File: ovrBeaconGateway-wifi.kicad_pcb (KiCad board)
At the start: 2 copper layers, 78 x 78 mm, 39 parts, among them J1 USB_MICROB_RA_LONG, J2 CONN_RJ45_RA, Q1 BJT_NPN_1.5A_25V, Q2 BJT_NPN_1.5A_25V, Q3 FET_NP_5A/3A_60V, U1 SILICONLABS_SI7050, U2 TOREX_XC6210, U3 FTDI_RT232RL, U4 ESP32-WROOM, U5 INTERSIL_ISL32602EFBZ

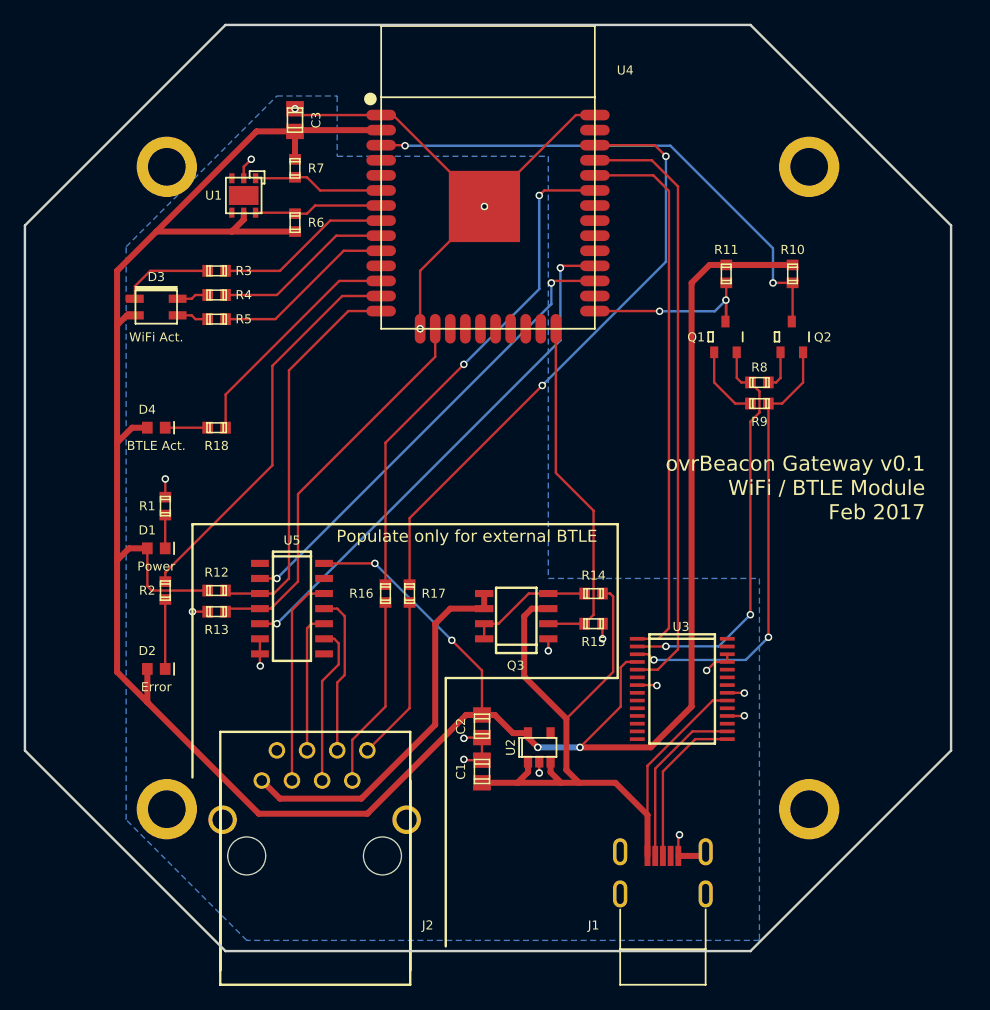
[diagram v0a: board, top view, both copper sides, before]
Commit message: Included an optional BLE121 on this module to allow for stand-alone long range operation
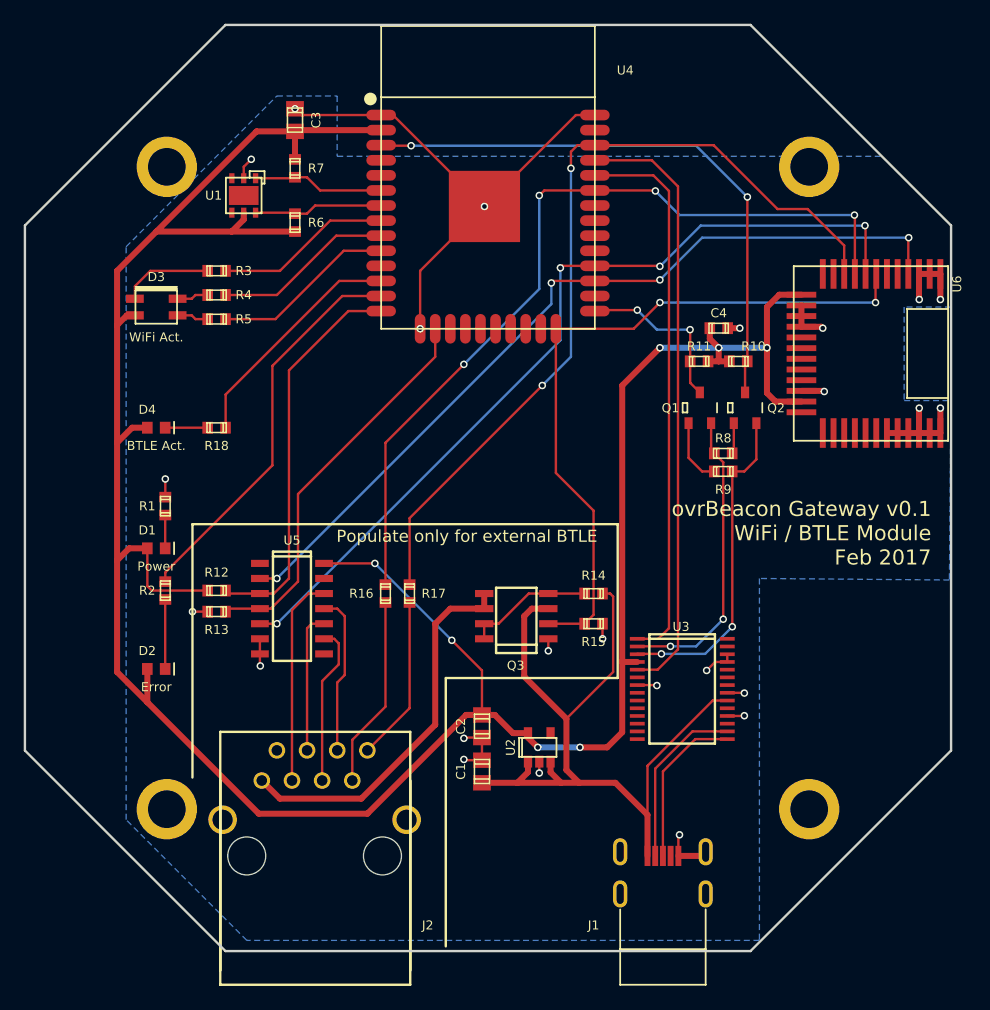
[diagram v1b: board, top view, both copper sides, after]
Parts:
- added C4: C_0.1uF_10v_0603, ovrEngineered:C_0603, F.Cu at (146.4, 62.7)
- added U6: BLUEGIGA_BLE121, ovrEngineered:BLE121, F.Cu at (165.1, 58.4)
- moved R10 8.67 mm to (148.1, 65.5), turned to 180 degrees
- moved R11 7.71 mm to (144.8, 65.5), turned to 0 degrees
- moved Q2 7.15 mm to (147.7, 70.7)
- moved R8 6.70 mm to (146.8, 73.3)
- moved R9 6.48 mm to (146.8, 74.8)
- moved Q1 6.35 mm to (143.9, 70.7)
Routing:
- net /ESP32-TX_BTLE-RX: track 39.6 -> 70.6 mm, vias 2 -> 4
- net /BTLE_POWER_ENABLE: track 29.5 -> 59.8 mm, vias 0 -> 2
- net /ESP32-RX_BTLE-TX: track 44.3 -> 72.5 mm, vias 2 -> 4
- net /ESP32-RTS_BTLE-CTS: track 43.0 -> 70.7 mm, vias 2 -> 4
- net GND: track 71.2 -> 92.7 mm, vias 17 -> 24
- net /ESP32-CTS_BTLE-RTS: track 51.4 -> 71.2 mm
- net Net-(Q2-Pad2): track 37.9 -> 27.6 mm
- net Net-(Q1-Pad2): track 34.3 -> 25.1 mm
- net /ESP32_EN: track 44.5 -> 49.3 mm
- net /ESP32_IO0: track 16.5 -> 14.4 mm
- net +3V3: track 231.0 -> 232.4 mm, vias 4 -> 7
- net Net-(Q1-Pad1): track 6.33 -> 5.56 mm
- net Net-(Q2-Pad1): track 3.34 -> 2.60 mm

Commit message: Initial commit of second revision changes
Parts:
- removed D3: CREE_CLV1A_FKB, ovrEngineered:CREE_CLV1A_FKB
- removed D4: LED_BLUE_0603, ovrEngineered:D_0603
- added J3: CONN_DBG_PDI, ovrEngineered:TC2030-IDC, F.Cu at (142.2, 51.6)
- added J4: CONN_1.27MM_5X2, ovrEngineered:20021111-00010T4LF, F.Cu at (151.1, 91.4)
- added R19: R_0_0603, ovrEngineered:R_0603, F.Cu at (144.8, 77.7)
- added R20: R_0_0603, ovrEngineered:R_0603, F.Cu at (146.3, 77.7)
- added R21: R_0_0603, ovrEngineered:R_0603, F.Cu at (109.5, 84.1)
- added R22: R_0_0603, ovrEngineered:R_0603, F.Cu at (151.9, 62.0)
- added REF**: LIGHTPIPE_VLP-XXX, ovrEngineered:LIGHTPIPE_VLP-XXX, F.Cu at (99.9, 61.0)
- added REF**: LIGHTPIPE_VLP-XXX, ovrEngineered:LIGHTPIPE_VLP-XXX, F.Cu at (99.8, 71.1)
- added REF**: LIGHTPIPE_VLP-XXX, ovrEngineered:LIGHTPIPE_VLP-XXX, F.Cu at (99.9, 91.3)
- added SW1: ESWITCH_TL3315NF100Q, ovrEngineered:TL3315NF100Q, F.Cu at (99.9, 81.3)
- added U7: LITEON_LTR-329ALS, ovrEngineered:LITEON_LTR-329ALS, F.Cu at (99.9, 91.4)
- D1: value LED_GREEN_0603 -> CREE_CLV1A_FKB; footprint ovrEngineered:D_0603 -> ovrEngineered:CREE_CLV1A_FKB
- D2: value LED_RED_0603 -> CREE_CLV1A_FKB; footprint ovrEngineered:D_0603 -> ovrEngineered:CREE_CLV1A_FKB
- J1, J2: moved to B.Cu
- R1: value R_402_1%_0603 -> R_12K_1%_0603
- R11: value R_5.1K_1%_0603 -> R_12K_1%_0603
- R18: value R_402_1%_0603 -> R_10K_1%_0603
- R6, R7: value R_10K_1%_0603 -> R_402_1%_0603
- moved R18 48.1 mm to (151.9, 65.3), turned to 0 degrees
- moved U1 45.2 mm to (99.9, 96.3), turned to 90 degrees
- moved D2 30.5 mm to (99.9, 61.0)
- moved R2 22.1 mm to (106.9, 63.9), turned to 180 degrees
- moved U6 20.0 mm to (156.0, 76.2)
- moved Q1 19.7 mm to (134.1, 87.9)
- moved Q2 18.4 mm to (141.0, 87.9)
- moved R14 17.9 mm to (118.0, 84.1), turned to 270 degrees
- moved R8 16.8 mm to (138.4, 87.9)
- moved R15 16.5 mm to (119.8, 84.1), turned to 270 degrees
- moved C2 16.1 mm to (130.4, 111.9)
- moved R9 14.3 mm to (138.4, 86.4)
- moved R1 14.2 mm to (106.9, 65.4), turned to 180 degrees
- moved C1 13.4 mm to (132.7, 111.9), turned to 90 degrees
- moved R17 12.6 mm to (107.8, 84.1)
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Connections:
- net /+5V_SWITCHED renamed Net-(J2-Pad1)
- D1 pad 1: +3V3 -> Net-(D1-Pad1)
- D1 pad 2: Net-(D1-Pad2) -> +3V3
- D2 pad 1: +3V3 -> Net-(D2-Pad1)
- D2 pad 2: Net-(D2-Pad2) -> +3V3
- R1 pad 1: Net-(D1-Pad2) -> +3V3
- R1 pad 2: GND -> /SW_WIFI_PROV
- R12 pad 2: /~422_RE -> /SDA_BLE121
- R13 pad 1: /422_DE -> +3V3
- R13 pad 2: GND -> /SCL_BLE121
- R14 pad 1: +5V -> Net-(Q3-Pad4)
- R14 pad 2: Net-(Q3-Pad4) -> +5V
- R18 pad 1: Net-(D4-Pad2) -> /~BLE121_RESET
- R18 pad 2: /LED_BTLE_ACT -> /BTLE_POWER_ENABLE
- R2 pad 1: Net-(D2-Pad2) -> Net-(D1-Pad1)
- R2 pad 2: /LED_ERROR -> /LED_WIFI_R
- R3 pad 1: Net-(D3-Pad1) -> Net-(D1-Pad4)
- R3 pad 2: /LED_RGB_R -> /LED_WIFI_G
- R4 pad 1: Net-(D3-Pad4) -> Net-(D1-Pad3)
- R4 pad 2: /LED_RGB_G -> /LED_WIFI_B
- R5 pad 1: Net-(D3-Pad3) -> Net-(D2-Pad1)
- R5 pad 2: /LED_RGB_B -> /LED_BTLE_R
- R6 pad 1: +3V3 -> Net-(D2-Pad4)
- R6 pad 2: /SCL -> /LED_BTLE_G
- R7 pad 1: +3V3 -> Net-(D2-Pad3)
- R7 pad 2: /SDA -> /LED_BTLE_B
- U1 pad 1: /SDA -> /SDA_BLE121
- U1 pad 6: /SCL -> /SCL_BLE121
- U4 pad 10: /LED_RGB_B -> /LED_WIFI_B
- U4 pad 11: (no net) -> /LED_WIFI_R
- U4 pad 12: /LED_BTLE_ACT -> /SW_WIFI_PROV
- U4 pad 13: /LED_ERROR -> /ESP32-CTS_BTLE-RTS
- U4 pad 14: /~422_RE -> /~VAR_EXT
- U4 pad 16: /422_DE -> /ESP32-RTS_BTLE-CTS
- U4 pad 24: /BTLE_POWER_ENABLE -> (no net)
- U4 pad 26: (no net) -> /BTLE_POWER_ENABLE
- U4 pad 27: /ESP32-TX_BTLE-RX -> /ESP32-RX_BTLE-TX
- U4 pad 28: /ESP32-RX_BTLE-TX -> /ESP32-TX_BTLE-RX
- U4 pad 30: (no net) -> /~VAR_IHP
- U4 pad 31: (no net) -> /SDA_ESP32
- U4 pad 33: /ESP32-RTS_BTLE-CTS -> /SCL_ESP32
- U4 pad 36: /ESP32-CTS_BTLE-RTS -> (no net)
- U4 pad 6: /SDA -> /LED_BTLE_G
- U4 pad 7: /SCL -> /LED_BTLE_B
- U4 pad 8: /LED_RGB_R -> /LED_BTLE_R
- U4 pad 9: /LED_RGB_G -> /LED_WIFI_G
- U5 pad 2: /ESP32-TX_BTLE-RX -> /ESP32-RX_BTLE-TX
- U5 pad 3: /~422_RE -> GND
- U5 pad 4: /422_DE -> +3V3
- U5 pad 5: /ESP32-RX_BTLE-TX -> /ESP32-TX_BTLE-RX
- U6 pad 20: (no net) -> /P2_1/PROG
- U6 pad 21: (no net) -> /P2_2/PROG
- U6 pad 24: (no net) -> /SCL_BLE121
- U6 pad 25: (no net) -> /SDA_BLE121
- U6 pad 7: /BTLE_POWER_ENABLE -> /~BLE121_RESET
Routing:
- net +3V3: track 232.4 -> 38.0 mm, vias 7 -> 8
- net /SDA_BLE121: track 0.00 -> 79.0 mm, vias 0 -> 4
- net /SCL_BLE121: track 0.00 -> 70.6 mm, vias 0 -> 2
- net GND: track 92.7 -> 137.1 mm, vias 24 -> 38
- net /~BLE121_RESET: track 0.00 -> 41.0 mm, vias 0 -> 2
- net /ESP32_IO0: track 14.4 -> 51.0 mm
- net /LED_ERROR: track 33.5 -> 0.00 mm
- net /~422_RE: track 33.3 -> 0.00 mm
- net /422_DE: track 33.2 -> 0.00 mm
- net /SW_WIFI_PROV: track 0.00 -> 31.9 mm
- net /SCL_ESP32: track 0.00 -> 29.8 mm, vias 0 -> 2
- net /SDA_ESP32: track 0.00 -> 27.1 mm, vias 0 -> 2
- net Net-(J2-Pad1): track 32.2 -> 9.05 mm
- net /~VAR_EXT: track 0.00 -> 23.1 mm
- net /LED_BTLE_ACT: track 19.9 -> 0.00 mm
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- added copper zone on F.Cu, net +3V3
- added copper zone on F.Cu, net GND
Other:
- board size 78 x 78 mm -> 71.1 x 72.9 mm
- board text added: "BTLE Activity"
- board text added: "External BTLE Only"
- board text added: "Internal + Internal High-Power BTLE Only"
- board text added: "Internal BTLE Only"
- board text added: "Internal High-Power BTLE Only"
- board text added: "On-board Prog. Only"
- board text added: "WiFi Activity"
- board text added: "WiFi Provision"
- board text added: "ovrBeacon Gateway v0.2 Apr 2017"
- board text removed: "BTLE Act."
- board text removed: "Error"
- board text removed: "Populate only for external BTLE"
- board text removed: "Power"
- board text removed: "WiFi Act."
- board text removed: "ovrBeacon Gateway v0.1 WiFi / BTLE Module Feb 2017"
